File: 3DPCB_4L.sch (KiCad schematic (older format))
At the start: 196 parts, among them IC1 A5984_LP, IC2 A5984_LP, IC3 A5984_LP, IC4 A5984_LP, IC5 A5984_LP, IC6 MP9943, J10 , J11 , J12 , J13 , J14 , J15 , J16 , J2 , J3 , J4 , J5 , J6 , J7 , J8 , J9 , K1 CONN_3, K2 CONN_3, K3 CONN_3, K4 CONN_3, K5 CONN_3, K6 CONN_3, K7 CONN_3, K8 CONN_3, K9 CONN_3, P1 CONN_8, P11 CONN_3X2, P12 CONN_3X2, P13 CONN_4, P2 CONN_8, P3 CONN_01X02, P5 CONN_4, P6 CONN_4, P7 CONN_4, P8 CONN_02X03, P9 CONN_4, U1 CONN_4_LERCHE, U10 MICRO-SD, U11 TC4427, U12 MCP4728, U13 CONN_4_LERCHE, U15 SPST_MOMENTARY, U16 CONN_4_LERCHE, U2 SPST_MOMENTARY, U21 CONN_4_LERCHE, U22 CONN_4_LERCHE, U23 MCP4728, U24 IRFH5302, U25 CONN_4_LERCHE, U3 BSS84, U4 CONN_4_LERCHE, U5 IRFH5302, U6 LPC1768_TQFP100, U7 IRFH5302, U8 IRFH5302, U9 TC4427

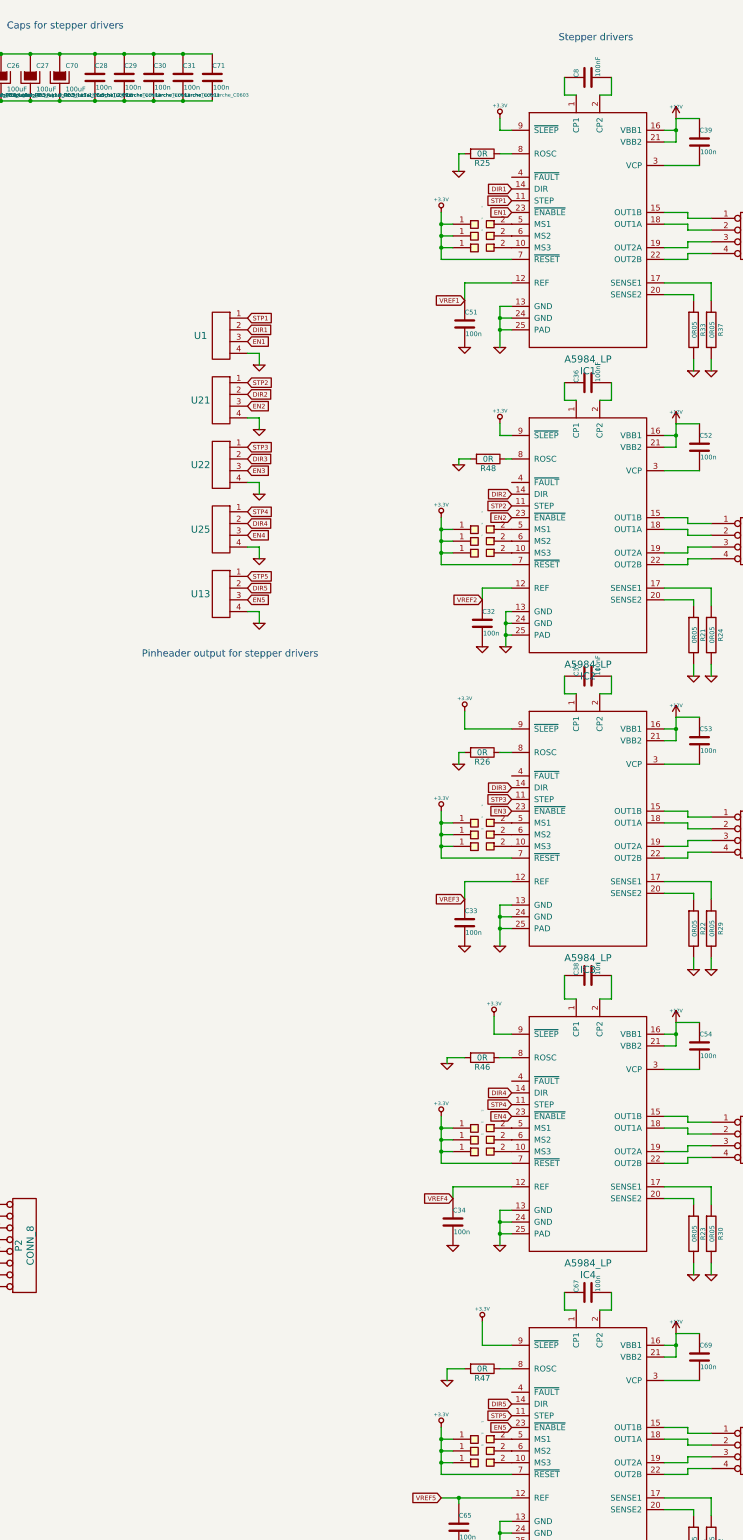
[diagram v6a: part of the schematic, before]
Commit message: A4982/A5984 compatible
Now it's possible to use both stepper drivers. Everything else is the
same. PCB's will be produced within a short timespan.
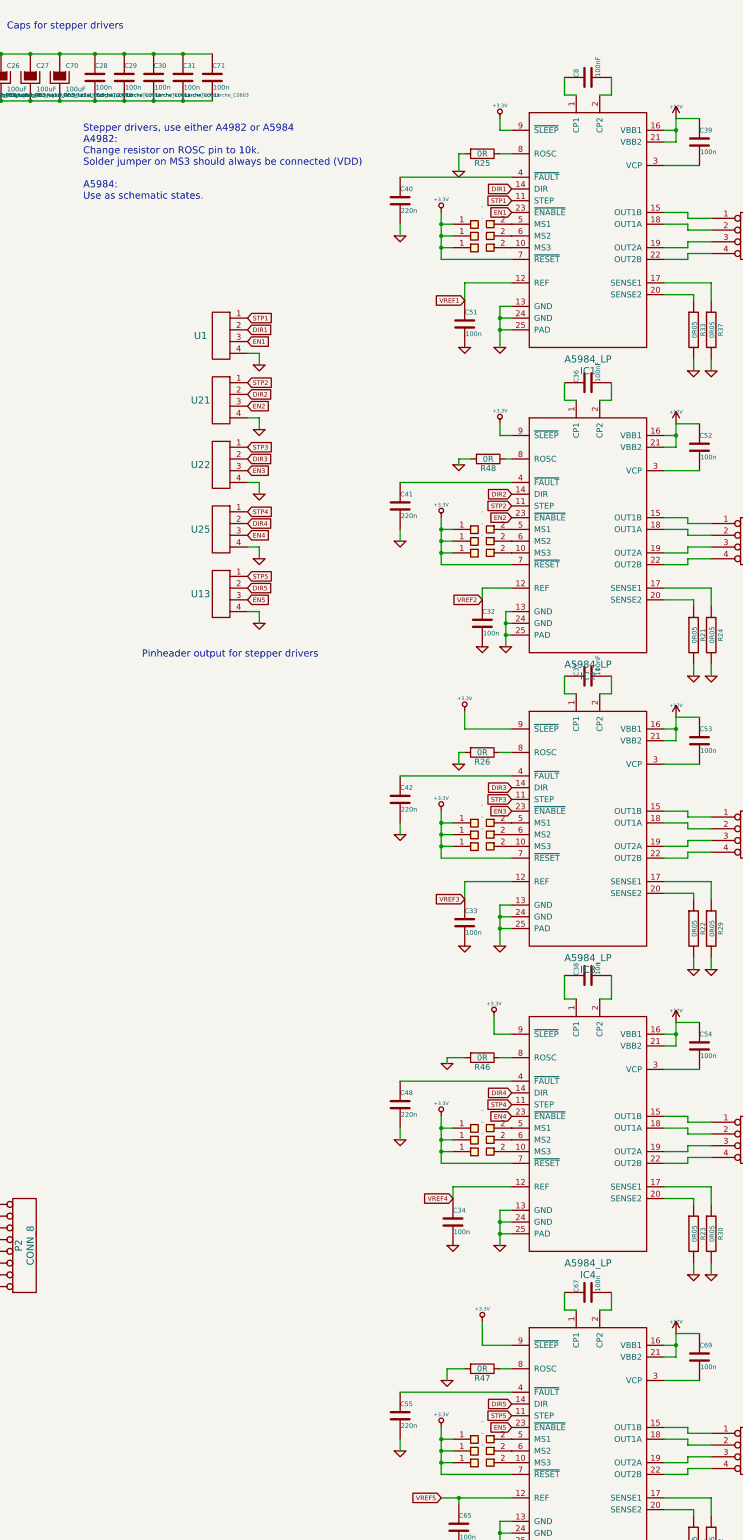
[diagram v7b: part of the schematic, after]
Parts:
- added C40, C41, C42, C48, C55: 220n, LercheTech:Lerche_C0603, symbol C-RESCUE-3DPCB_4L
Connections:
- net GND: now also C40.2, C41.2, C42.2, C48.2, C55.2
- net at IC5.4 (~FAULT): now also C55.1
- net at IC4.4 (~FAULT): now also C48.1
- net at IC3.4 (~FAULT): now also C42.1
- net at IC2.4 (~FAULT): now also C41.1
- net at IC1.4 (~FAULT): now also C40.1
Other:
- note added: "Stepper drivers, use either A4982 or A5984\nA4982:\nChange resistor on ROSC pin to 10k.\nSolder jumper on MS3 should always be connected (VDD)\n\nA5984:\nUse as schematic states. \n"
- note removed: "Stepper drivers"
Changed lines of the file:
@@
 Text Notes 16900 6100 0    60   ~ 0
 Pinheader output for stepper drivers
-Text Notes 20450 850  0    60   ~ 0
-Stepper drivers
+Text Notes 16400 2200 0    60   ~ 0
+Stepper drivers, use either A4982 or A5984\nA4982:\nChange resistor on ROSC pin to 10k.\nSolder jumper on MS3 should always be connected (VDD)\n\nA5984:\nUse as schematic states. \n
 Text Notes 15750 750  0    60   ~ 0
 Caps for stepper drivers
@@
 	5000 5750 5000 5900
 Connection ~ 5000 5900
+$Comp
+L C-RESCUE-3DPCB_4L C40
+U 1 1 58B5A292
+P 19100 2200
+F 0 "C40" H 19100 2300 40  0000 L CNN
+F 1 "220n" H 19106 2115 40  0000 L CNN
+F 2 "LercheTech:Lerche_C0603" H 19138 2050 30  0001 C CNN
+F 3 "~" H 19100 2200 60  0000 C CNN
+	1    19100 2200
+	1    0    0    -1
+$EndComp
+Wire Wire Line
+	20050 2000 19100 2000
+$Comp
+L GND-RESCUE-3DPCB_4L #PWR0136
+U 1 1 58B5A993
+P 19100 2500
+F 0 "#PWR0136" H 19100 2500 30  0001 C CNN
+F 1 "GND" H 19100 2430 30  0001 C CNN
+F 2 "" H 19100 2500 60  0000 C CNN
+F 3 "" H 19100 2500 60  0000 C CNN
+	1    19100 2500
+	1    0    0    -1
+$EndComp
+Wire Wire Line
+	19100 2500 19100 2400
+$Comp
+L C-RESCUE-3DPCB_4L C41
+U 1 1 58B5B680
+P 19100 4800
+F 0 "C41" H 19100 4900 40  0000 L CNN
+F 1 "220n" H 19106 4715 40  0000 L CNN
+F 2 "LercheTech:Lerche_C0603" H 19138 4650 30  0001 C CNN
+F 3 "~" H 19100 4800 60  0000 C CNN
+	1    19100 4800
+	1    0    0    -1
+$EndComp
+Wire Wire Line
+	20050 4600 19100 4600
+$Comp
+L GND-RESCUE-3DPCB_4L #PWR0137
+U 1 1 58B5D5A8
+P 19100 5100
+F 0 "#PWR0137" H 19100 5100 30  0001 C CNN
+F 1 "GND" H 19100 5030 30  0001 C CNN
+F 2 "" H 19100 5100 60  0000 C CNN
+F 3 "" H 19100 5100 60  0000 C CNN
+	1    19100 5100
+	1    0    0    -1
+$EndComp
+Wire Wire Line
+	19100 5100 19100 5000
+$Comp
+L C-RESCUE-3DPCB_4L C42
+U 1 1 58B5DB46
+P 19100 7300
+F 0 "C42" H 19100 7400 40  0000 L CNN
+F 1 "220n" H 19106 7215 40  0000 L CNN
+F 2 "LercheTech:Lerche_C0603" H 19138 7150 30  0001 C CNN
+F 3 "~" H 19100 7300 60  0000 C CNN
+	1    19100 7300
+	1    0    0    -1
+$EndComp
+Wire Wire Line
+	20050 7100 19100 7100
+$Comp
+L GND-RESCUE-3DPCB_4L #PWR0138
+U 1 1 58B601B2
+P 19100 7600
+F 0 "#PWR0138" H 19100 7600 30  0001 C CNN
+F 1 "GND" H 19100 7530 30  0001 C CNN
+F 2 "" H 19100 7600 60  0000 C CNN
+F 3 "" H 19100 7600 60  0000 C CNN
+	1    19100 7600
+	1    0    0    -1
+$EndComp
+Wire Wire Line
+	19100 7600 19100 7500
+$Comp
+L C-RESCUE-3DPCB_4L C48
+U 1 1 58B6132C
+P 19100 9900
+F 0 "C48" H 19100 10000 40  0000 L CNN
+F 1 "220n" H 19106 9815 40  0000 L CNN
+F 2 "LercheTech:Lerche_C0603" H 19138 9750 30  0001 C CNN
+F 3 "~" H 19100 9900 60  0000 C CNN
+	1    19100 9900
+	1    0    0    -1
+$EndComp
+Wire Wire Line
+	20050 9700 19100 9700
+$Comp
+L GND-RESCUE-3DPCB_4L #PWR0139
+U 1 1 58B632EE
+P 19100 10200
+F 0 "#PWR0139" H 19100 10200 30  0001 C CNN
+F 1 "GND" H 19100 10130 30  0001 C CNN
+F 2 "" H 19100 10200 60  0000 C CNN
+F 3 "" H 19100 10200 60  0000 C CNN
+	1    19100 10200
+	1    0    0    -1
+$EndComp
+Wire Wire Line
+	19100 10200 19100 10100
+$Comp
+L C-RESCUE-3DPCB_4L C55
+U 1 1 58B63D7F
+P 19100 12550
+F 0 "C55" H 19100 12650 40  0000 L CNN
+F 1 "220n" H 19106 12465 40  0000 L CNN
+F 2 "LercheTech:Lerche_C0603" H 19138 12400 30  0001 C CNN
+F 3 "~" H 19100 12550 60  0000 C CNN
+	1    19100 12550
+	1    0    0    -1
+$EndComp
+Wire Wire Line
+	20050 12350 19100 12350
+$Comp
+L GND-RESCUE-3DPCB_4L #PWR0140
+U 1 1 58B65841
+P 19100 12850
+F 0 "#PWR0140" H 19100 12850 30  0001 C CNN
+F 1 "GND" H 19100 12780 30  0001 C CNN
+F 2 "" H 19100 12850 60  0000 C CNN
+F 3 "" H 19100 12850 60  0000 C CNN
+	1    19100 12850
+	1    0    0    -1
+$EndComp
+Wire Wire Line
+	19100 12850 19100 12750
 $EndSCHEMATC

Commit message: Working files.
Tested, working!
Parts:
- L1, L2: symbol INDUCTOR -> INDUCTOR-RESCUE-3DPCB_4L
- U12, U23: symbol MCP4728 -> MCP4728-RESCUE-3DPCB_4L
- U3: symbol BSS84 -> BSS84-RESCUE-3DPCB_4L
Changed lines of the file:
@@
 $EndComp
 $Comp
-L INDUCTOR L1
+L INDUCTOR-RESCUE-3DPCB_4L L1
 U 1 1 524AC987
 P 5150 6400
@@
 SCL
 $Comp
-L BSS84 U3
+L BSS84-RESCUE-3DPCB_4L U3
 U 1 1 524B1CD6
 P 2500 5900
@@
 SCK1
 $Comp
-L INDUCTOR L2
+L INDUCTOR-RESCUE-3DPCB_4L L2
 U 1 1 5260BF3A
 P 2800 1450
@@
 VREF1
 $Comp
-L MCP4728 U23
+L MCP4728-RESCUE-3DPCB_4L U23
 U 1 1 5269312C
 P 13200 8350
@@
 $EndComp
 $Comp
-L MCP4728 U12
+L MCP4728-RESCUE-3DPCB_4L U12
 U 1 1 53E5DFFA
 P 13200 9150
